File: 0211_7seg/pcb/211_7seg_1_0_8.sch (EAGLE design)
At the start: 25 parts

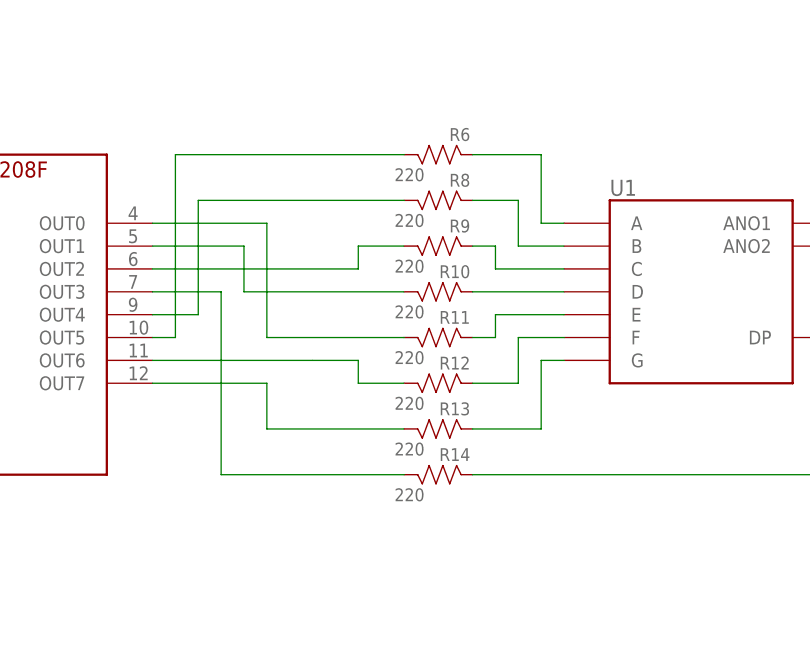
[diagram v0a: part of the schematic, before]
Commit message: #211 7Segment LED保護抵抗の変更 220->25
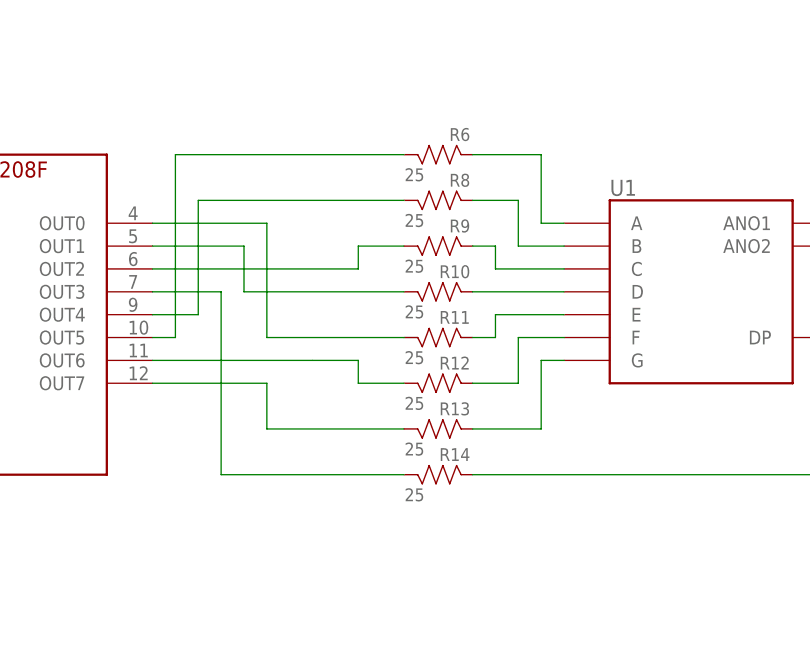
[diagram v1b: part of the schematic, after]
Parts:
- R10, R11, R12, R13, R14, R6, R8, R9: value 220 -> 25
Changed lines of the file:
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@@
 <?xml version="1.0" encoding="utf-8"?>
 <!DOCTYPE eagle SYSTEM "eagle.dtd">
-<eagle version="9.6.2">
+<eagle version="9.6.0">
 <drawing>
 <settings>
@@
 <setting verticaltext="up"/>
 </settings>
-<grid distance="0.1" unitdist="inch" unit="inch" style="lines" multiple="1" display="yes" altdistance="0.01" altunitdist="inch" altunit="inch"/>
+<grid distance="0.1" unitdist="inch" unit="inch" style="lines" multiple="1" display="no" altdistance="0.01" altunitdist="inch" altunit="inch"/>
 <layers>
 <layer number="1" name="Top" color="4" fill="1" visible="no" active="no"/>
@@
 <part name="R4" library="FaBo-Resistors" deviceset="RESISTOR" device="-0603" value="NC"/>
 <part name="GND6" library="FaBo-Supply" deviceset="GND" device=""/>
-<part name="R6" library="FaBo-Resistors" deviceset="RESISTOR" device="-0603" value="220"/>
-<part name="R8" library="FaBo-Resistors" deviceset="RESISTOR" device="-0603" value="220"/>
-<part name="R9" library="FaBo-Resistors" deviceset="RESISTOR" device="-0603" value="220"/>
-<part name="R10" library="FaBo-Resistors" deviceset="RESISTOR" device="-0603" value="220"/>
-<part name="R11" library="FaBo-Resistors" deviceset="RESISTOR" device="-0603" value="220"/>
-<part name="R12" library="FaBo-Resistors" deviceset="RESISTOR" device="-0603" value="220"/>
-<part name="R13" library="FaBo-Resistors" deviceset="RESISTOR" device="-0603" value="220"/>
-<part name="R14" library="FaBo-Resistors" deviceset="RESISTOR" device="-0603" value="220"/>
+<part name="R6" library="FaBo-Resistors" deviceset="RESISTOR" device="-0603" value="25"/>
+<part name="R8" library="FaBo-Resistors" deviceset="RESISTOR" device="-0603" value="25"/>
+<part name="R9" library="FaBo-Resistors" deviceset="RESISTOR" device="-0603" value="25"/>
+<part name="R10" library="FaBo-Resistors" deviceset="RESISTOR" device="-0603" value="25"/>
+<part name="R11" library="FaBo-Resistors" deviceset="RESISTOR" device="-0603" value="25"/>
+<part name="R12" library="FaBo-Resistors" deviceset="RESISTOR" device="-0603" value="25"/>
+<part name="R13" library="FaBo-Resistors" deviceset="RESISTOR" device="-0603" value="25"/>
+<part name="R14" library="FaBo-Resistors" deviceset="RESISTOR" device="-0603" value="25"/>
 <part name="LOGO1" library="component" deviceset="LOGO_FABO" device="-M"/>
 </parts>
